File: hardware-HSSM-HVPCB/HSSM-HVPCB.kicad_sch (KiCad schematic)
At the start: 44 parts, among them J1 2086-1103, J2 2601-1110, K1 G6DN-1A-L DC12, K2 G6DN-1A-L DC12, Q1 Q_NMOS_SOT-23_IRLML6344, Q2 Q_NMOS_SOT-23_IRLML6344, U1 LNK3204D-TL, U2 CS5480-INZ, U3 LTV-354T, U4 LTV-354T

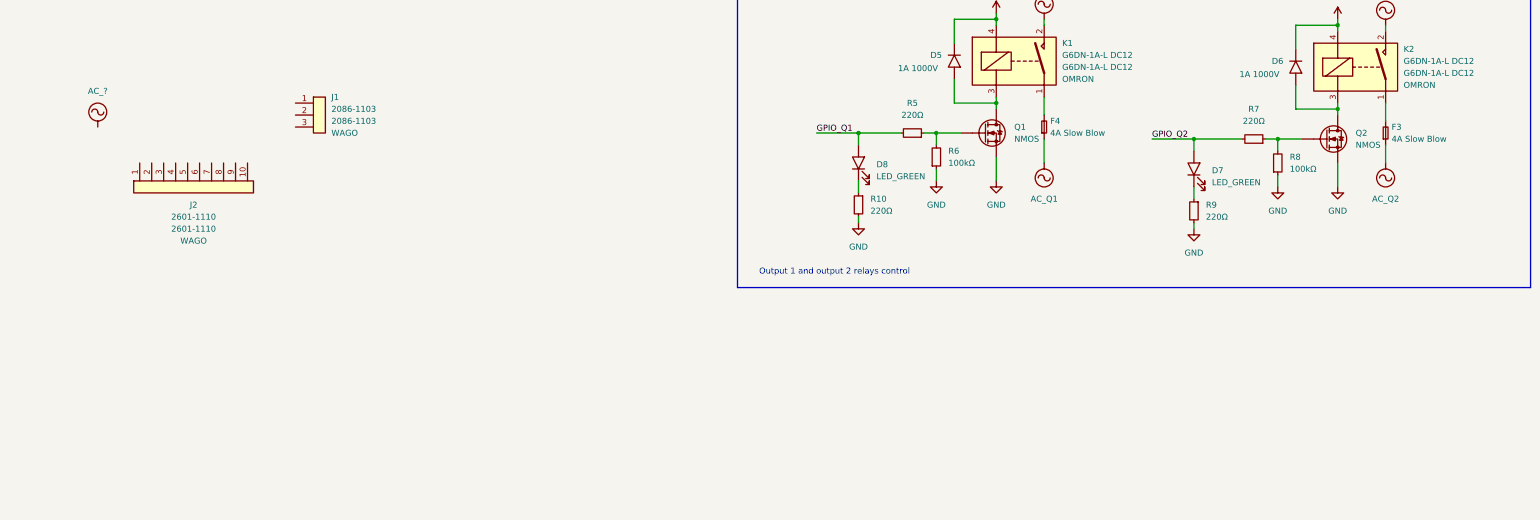
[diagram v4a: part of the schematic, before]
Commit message: [#3] Add HV output terminals connections proposition
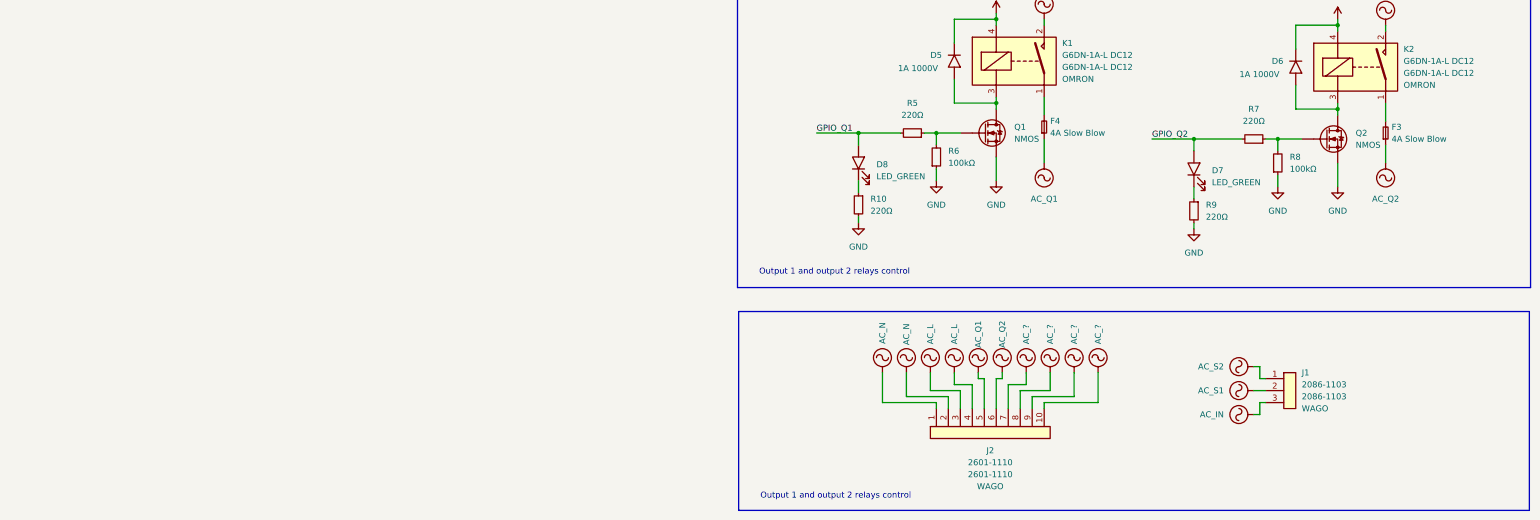
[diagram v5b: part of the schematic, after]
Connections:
- net AC_?: now also J2.10 (Pin_10), J2.7 (Pin_7), J2.8 (Pin_8), J2.9 (Pin_9)
- net AC_IN: now also J1.3 (Pin_3)
- net AC_N: now also J2.1 (Pin_1), J2.2 (Pin_2)
- net AC_Q1: now also J2.5 (Pin_5)
- net AC_Q2: now also J2.6 (Pin_6)
- net AC_S1: now also J1.2 (Pin_2)
- net AC_S2: now also J1.1 (Pin_1)
- net AC_L: now reaches J2.3 (Pin_3)
- net AC_L: now also J2.4 (Pin_4)
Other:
- moved on the sheet: J1, J2

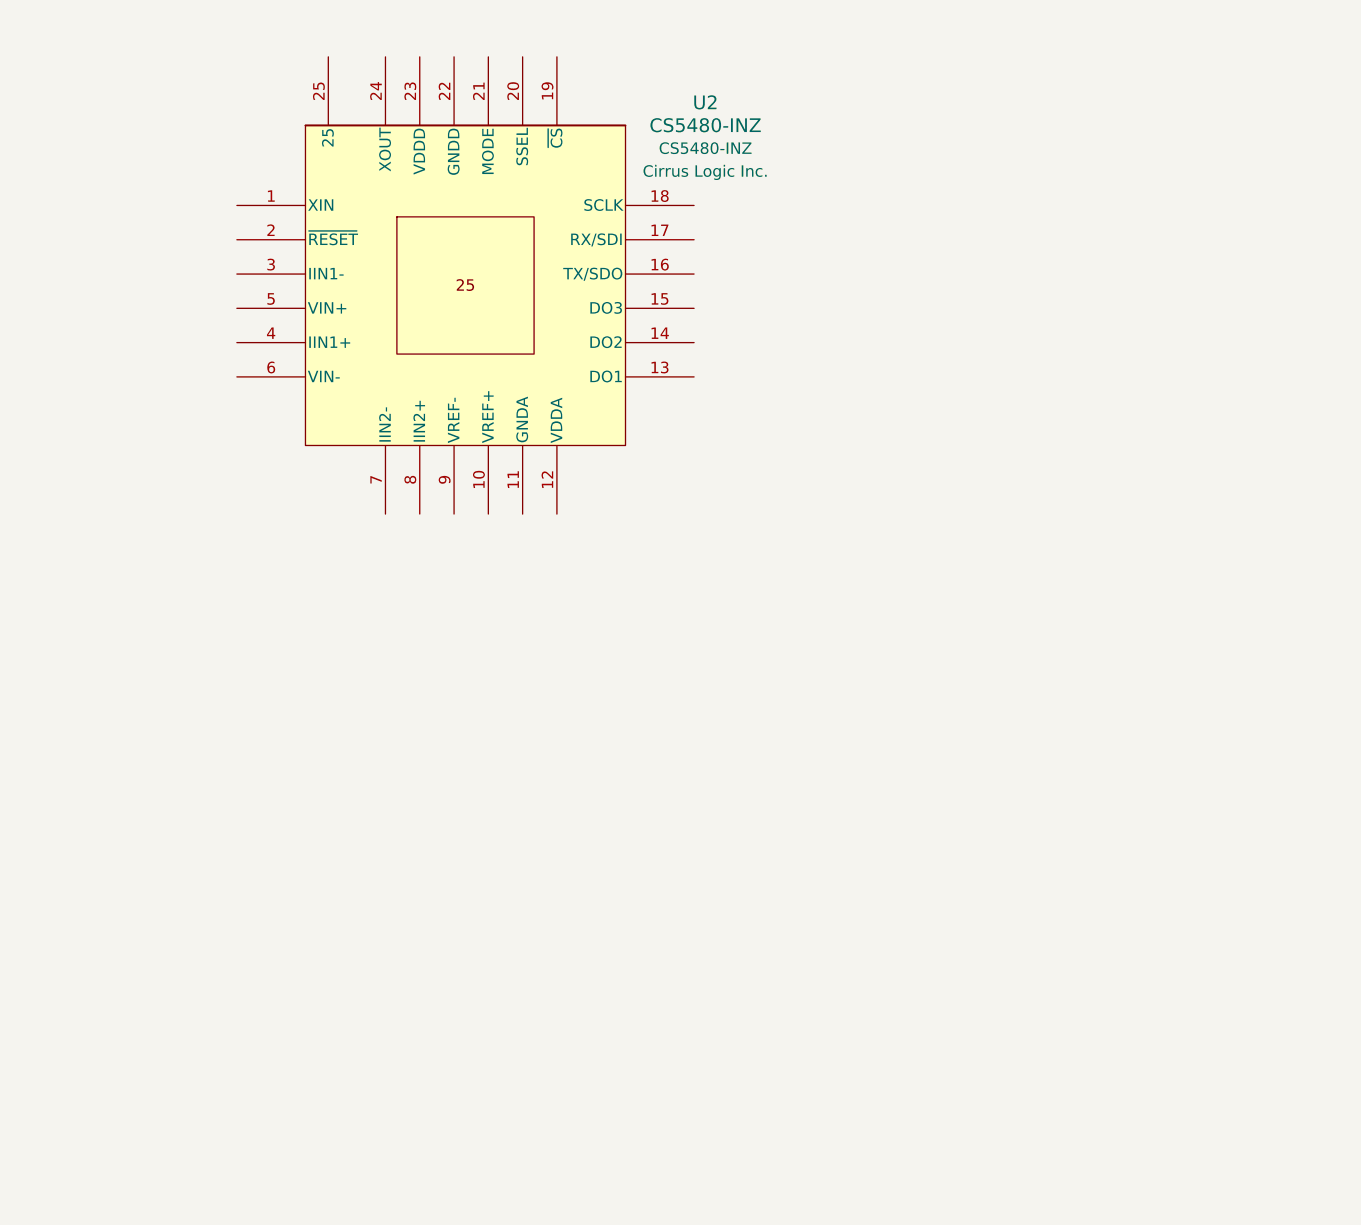
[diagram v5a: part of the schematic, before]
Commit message: [#3] SCH power measuring - voltage measure
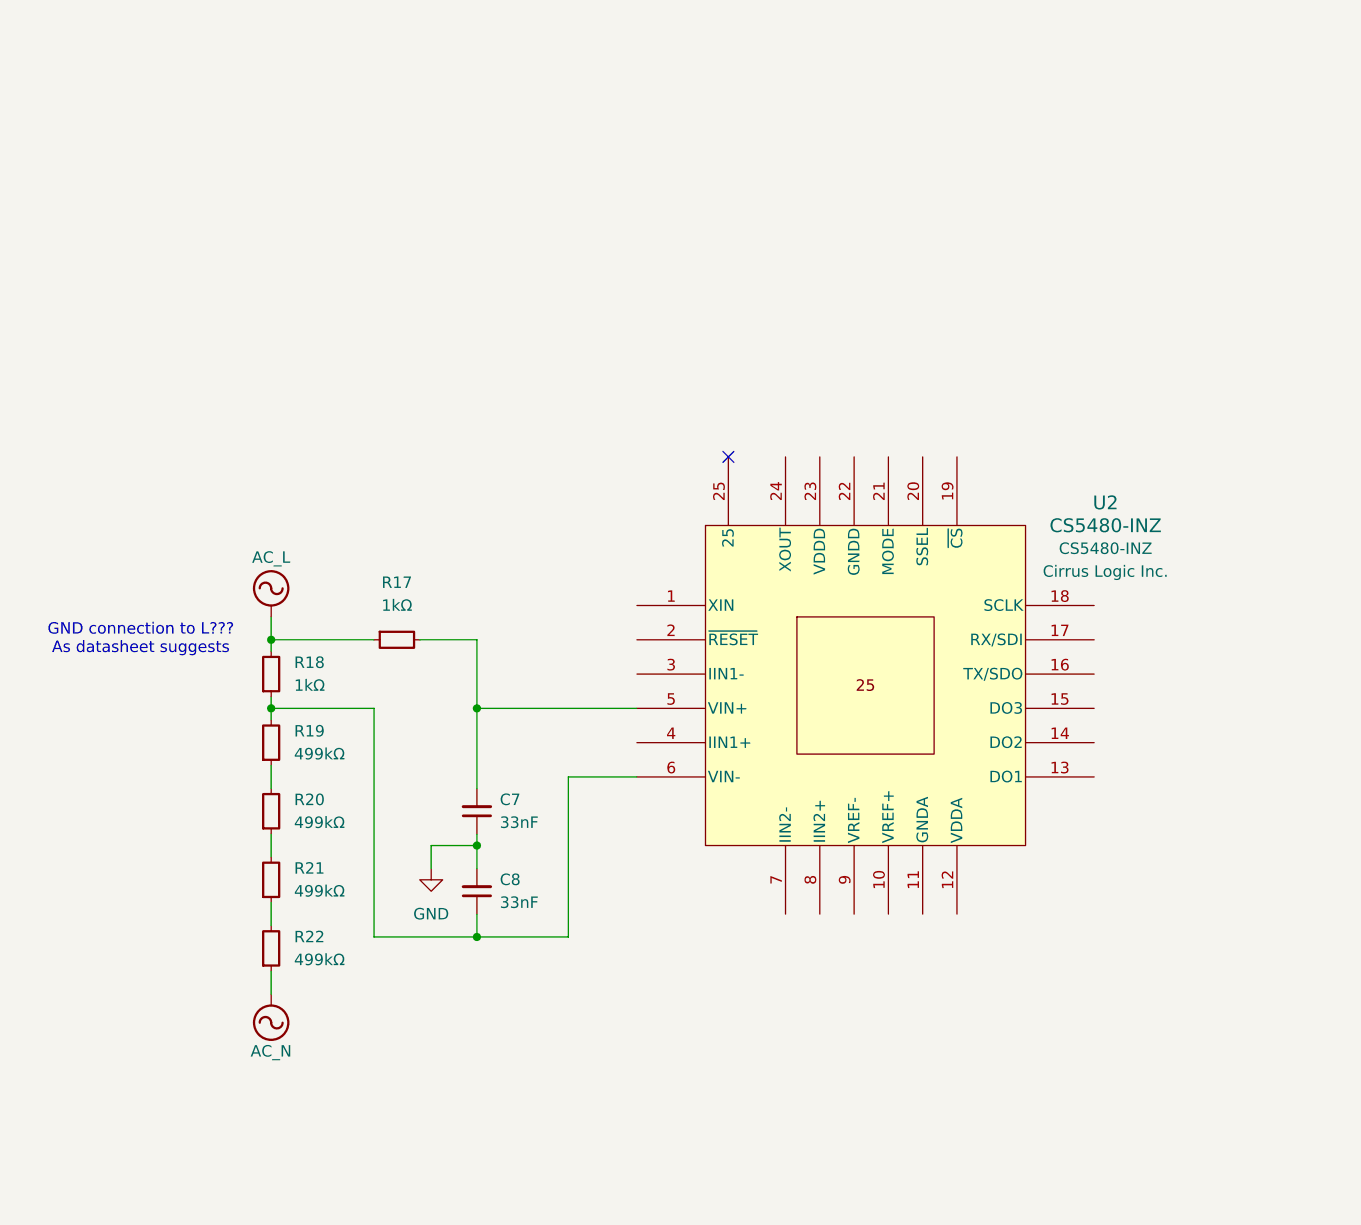
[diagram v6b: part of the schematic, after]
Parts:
- added C7, C8: C_33nF_10pct_50V_0402_CC0402KRX7R9BB333, HSSM-HVPCB:C_0402, symbol HSSM-HVPCB:C_33nF_10pct_50V_0402_CC0402KRX7R9BB333
- added R17, R18: R_1k_1pct_0402_CRCW04021K00FKED, HSSM-HVPCB:R_0402, symbol HSSM-HVPCB:R_1k_1pct_0402_CRCW04021K00FKED
- added R19, R20, R21, R22: R_499k_1pct_1206_KTR18EZPF4993, HSSM-HVPCB:R_1206, symbol HSSM-HVPCB:R_499k_1pct_1206_KTR18EZPF4993
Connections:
- net AC_L: now also R17.1, R18.2
- net AC_N: now also R22.1
- net GND: now also C7.1, C8.2
- net at U2.5 (VIN+): now also C7.2, R17.2
- net at U2.6 (VIN-): now also C8.1, R18.1, R19.2
- new net: R21.1, R22.2
- new net: R20.1, R21.2
- new net: R19.1, R20.2
- no-connect marks 0 -> 1
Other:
- note added: "GND connection to L??? As datasheet suggests"

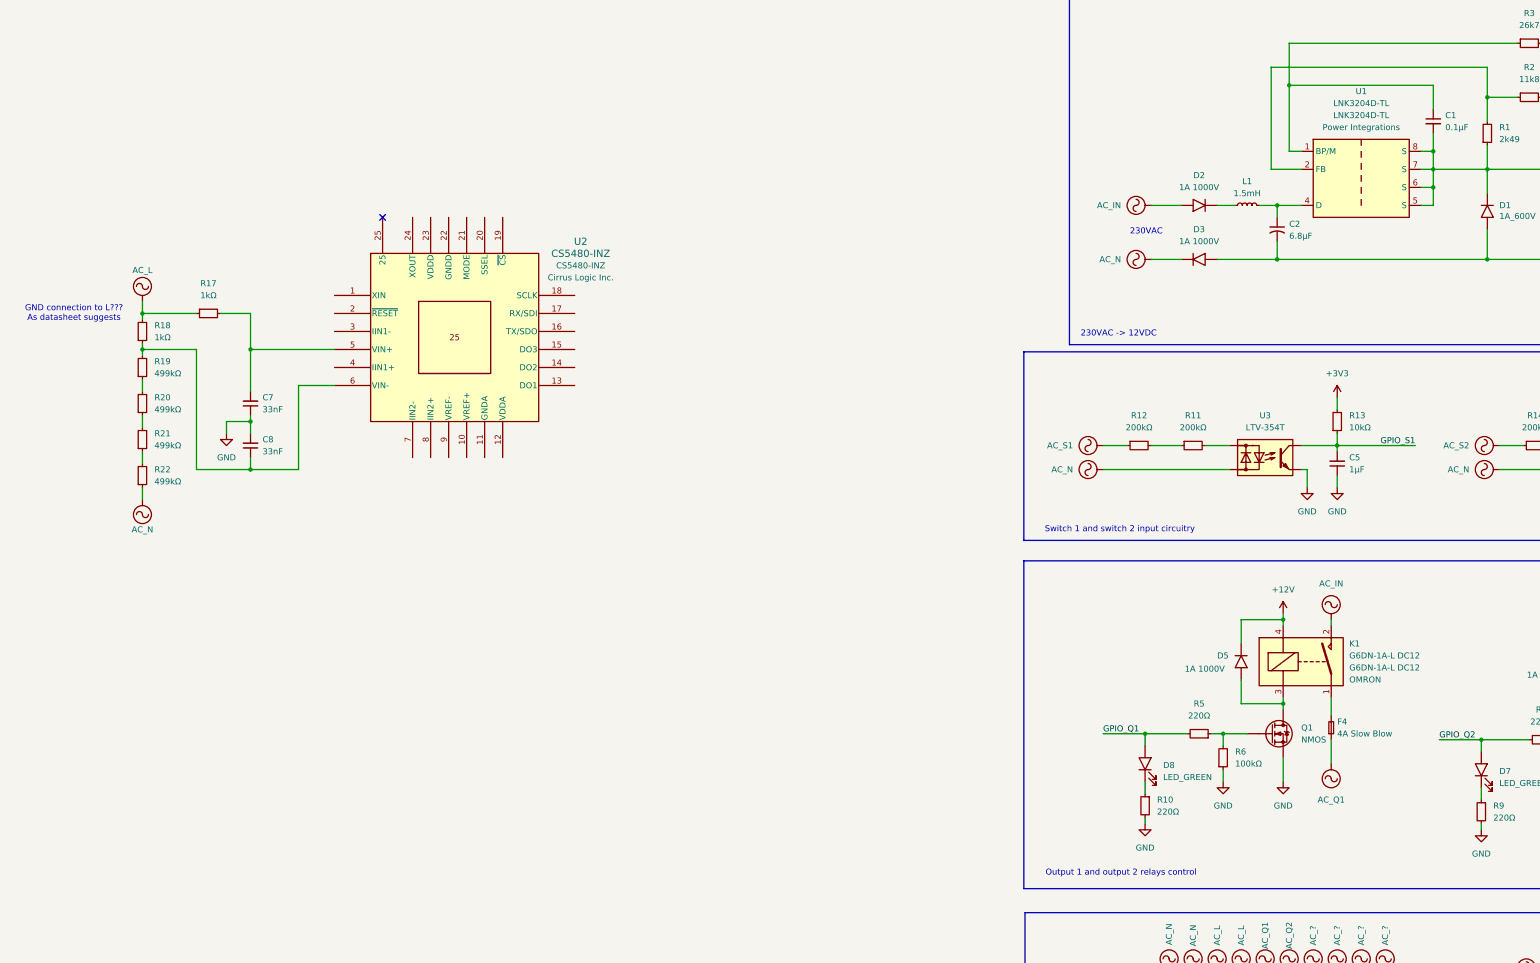
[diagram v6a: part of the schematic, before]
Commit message: [#3] SCH power measuring - current measure on CH1
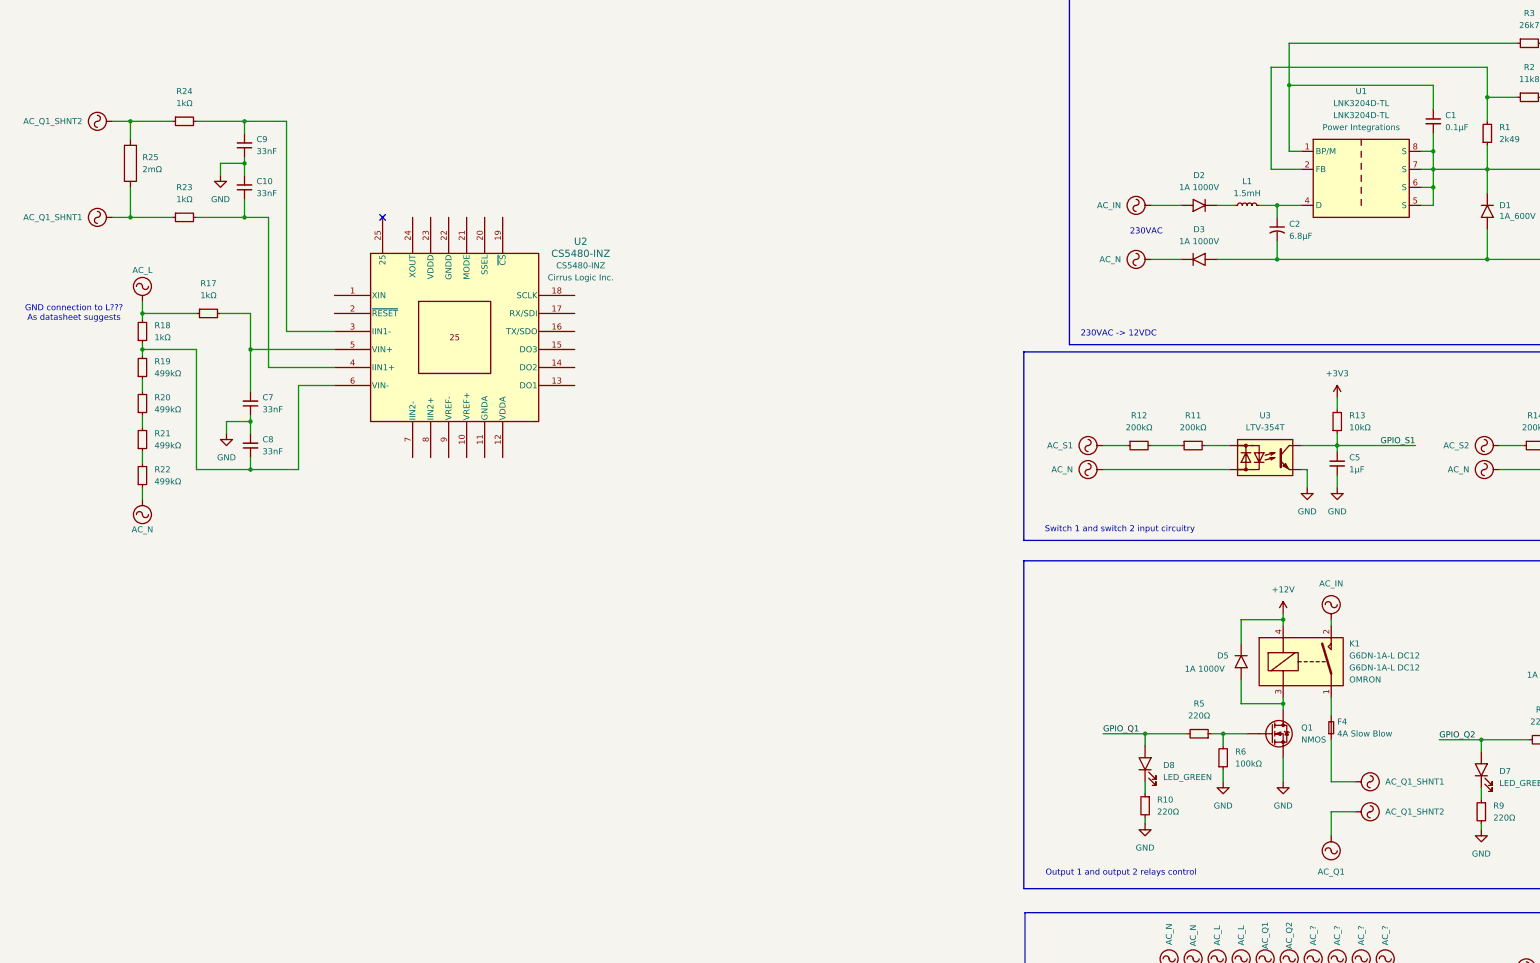
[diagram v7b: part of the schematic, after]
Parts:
- added C10, C9: C_33nF_10pct_50V_0402_CC0402KRX7R9BB333, HSSM-HVPCB:C_0402, symbol HSSM-HVPCB:C_33nF_10pct_50V_0402_CC0402KRX7R9BB333
- added R23, R24: R_1k_1pct_0402_CRCW04021K00FKED, HSSM-HVPCB:R_0402, symbol HSSM-HVPCB:R_1k_1pct_0402_CRCW04021K00FKED
- added R25: R_Shunt_2mOhm_1pct_2512_CRE2512-FZ-R002E-3, HSSM-HVPCB:R_2512, symbol HSSM-HVPCB:R_Shunt_2mOhm_1pct_2512_CRE2512-FZ-R002E-3
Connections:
- net AC_Q1: now also R24.1, R25.2; no longer F4.1
- net GND: now also C10.2, C9.1
- net at U2.3 (IIN1-): now also C9.2, R24.2
- net at U2.4 (IIN1+): now also C10.1, R23.2
- new net AC_Q1_SHNT1: F4.1, R23.1, R25.1

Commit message: [#3] SCH power measuring - current measure on CH2
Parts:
- added C11, C12: C_33nF_10pct_50V_0402_CC0402KRX7R9BB333, HSSM-HVPCB:C_0402, symbol HSSM-HVPCB:C_33nF_10pct_50V_0402_CC0402KRX7R9BB333
- added R26: R_Shunt_2mOhm_1pct_2512_CRE2512-FZ-R002E-3, HSSM-HVPCB:R_2512, symbol HSSM-HVPCB:R_Shunt_2mOhm_1pct_2512_CRE2512-FZ-R002E-3
- added R27, R28: R_1k_1pct_0402_CRCW04021K00FKED, HSSM-HVPCB:R_0402, symbol HSSM-HVPCB:R_1k_1pct_0402_CRCW04021K00FKED
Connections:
- net AC_Q2: now also R26.2, R27.1; no longer F3.1
- net GND: now also C11.1, C12.2
- net at U2.7 (IIN2-): now also C11.2, R27.2
- net at U2.8 (IIN2+): now also C12.1, R28.2
- new net AC_Q2_SHNT1: F3.1, R26.1, R28.1
